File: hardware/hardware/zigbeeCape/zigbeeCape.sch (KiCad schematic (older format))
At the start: 2 parts

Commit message: LIbrary updates
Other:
- moved on the sheet: U?A, U?B
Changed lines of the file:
@@
 L Zigbee:CC1352R U?
 U 2 1 6062844D
-P 1450 1750
-F 0 "U?" H 1675 2765 50  0000 C CNN
-F 1 "CC1352R" H 1675 2674 50  0000 C CNN
-F 2 "" H 2050 2950 50  0001 C CNN
-F 3 "" H 2050 2950 50  0001 C CNN
-	2    1450 1750
+P 2600 4900
+F 0 "U?" H 2825 5915 50  0000 C CNN
+F 1 "CC1352R" H 2825 5824 50  0000 C CNN
+F 2 "" H 3200 6100 50  0001 C CNN
+F 3 "" H 3200 6100 50  0001 C CNN
+	2    2600 4900
 	1    0    0    -1
 $EndComp
@@
 L Zigbee:CC1352R U?
 U 1 1 60629828
-P 2950 1750
-F 0 "U?" H 3400 2765 50  0000 C CNN
-F 1 "CC1352R" H 3400 2674 50  0000 C CNN
-F 2 "" H 3550 2950 50  0001 C CNN
-F 3 "" H 3550 2950 50  0001 C CNN
-	1    2950 1750
+P 2100 1800
+F 0 "U?" H 2550 2815 50  0000 C CNN
+F 1 "CC1352R" H 2550 2724 50  0000 C CNN
+F 2 "" H 2700 3000 50  0001 C CNN
+F 3 "" H 2700 3000 50  0001 C CNN
+	1    2100 1800
 	1    0    0    -1
 $EndComp
+$Comp
+L power:+3.3V #PWR?
+U 1 1 606286D5
+P 1250 2100
+F 0 "#PWR?" H 1250 1950 50  0001 C CNN
+F 1 "+3.3V" H 1265 2273 50  0000 C CNN
+F 2 "" H 1250 2100 50  0001 C CNN
+F 3 "" H 1250 2100 50  0001 C CNN
+	1    1250 2100
+	1    0    0    -1
+$EndComp

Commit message: Forgot a file
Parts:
- added C? (x3): C, symbol Device:C
- added D?: Green, symbol Device:LED
- added D? (x3): Blue, symbol Device:LED
- added D?: RED, symbol Device:LED
- added R? (x5): 1k, symbol Device:R
- added SW? (x3): SW_MEC_5E, symbol Switch:SW_MEC_5E
- added U?: BeagleBone_P8, symbol BeagleBone:BeagleBone_P8
- added U?: BeagleBone_P9, symbol BeagleBone:BeagleBone_P9
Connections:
- net +3V3: now also D?.2 (A)
- new net: D?.1 (K), R?.1 (x5)
- new net Check_Error: C?.1, SW?.3 (K), SW?.4 (A)
- new net Error: D?.2 (A)
- new net GND: C?.2, C?.2, C?.2, R?.2, R?.2, R?.2, R?.2, R?.2, SW?.1, SW?.1, SW?.1, SW?.2, SW?.2, SW?.2
- new net Network_Connect: C?.1, SW?.3 (K), SW?.4 (A)
- new net Server_Status: D?.2 (A)
- new net ZigBee_Connect: C?.1, SW?.3 (K), SW?.4 (A)
- new net ZigBee_Receive: D?.2 (A)
- new net ZigBee_Transmit: D?.2 (A)
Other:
- note added: "LEDs and Buttons"
- moved on the sheet: U?B

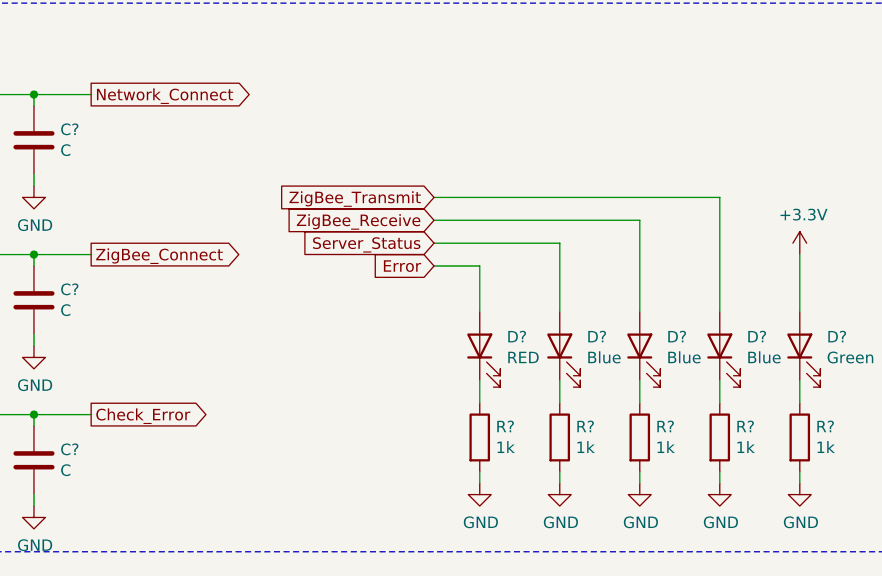
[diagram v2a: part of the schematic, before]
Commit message: Fixed LED names
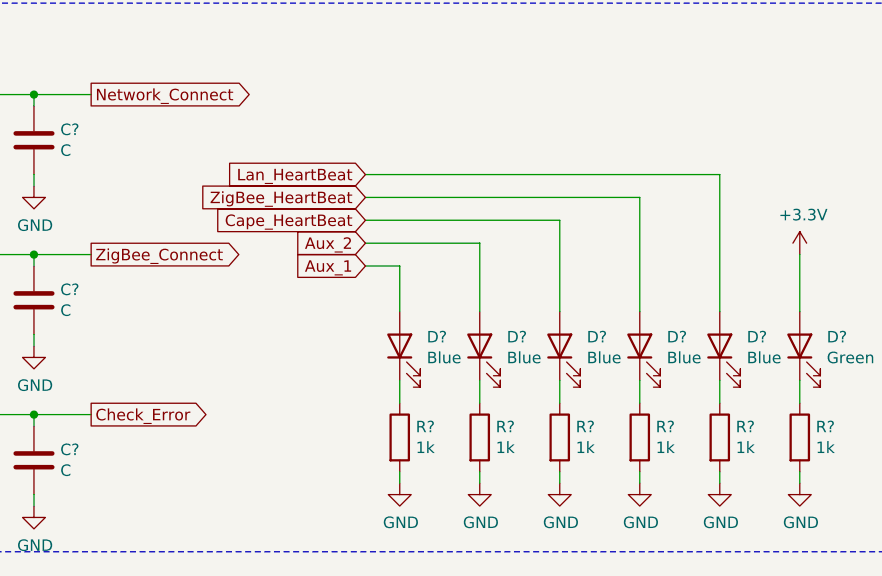
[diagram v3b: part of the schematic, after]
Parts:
- added D?: Blue, symbol Device:LED
- added R?: 1k, symbol Device:R
- D?: value RED -> Blue
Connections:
- net GND: now also R?.2
- net Error renamed Aux_2
- net Server_Status renamed Cape_HeartBeat
- net ZigBee_Receive renamed ZigBee_HeartBeat
- net ZigBee_Transmit renamed Lan_HeartBeat
- new net: D?.1 (K), R?.1
- new net Aux_1: D?.2 (A)
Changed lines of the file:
@@
 P 3600 6800
 F 0 "D?" V 3639 6682 50  0000 R CNN
-F 1 "RED" V 3548 6682 50  0000 R CNN
+F 1 "Blue" V 3548 6682 50  0000 R CNN
 F 2 "" H 3600 6800 50  0001 C CNN
 F 3 "~" H 3600 6800 50  0001 C CNN
@@
 	1650 7100 1900 7100
 Connection ~ 1650 7100
-Text GLabel 3400 6150 0    50   Input ~ 0
-ZigBee_Transmit
-Text GLabel 3400 6250 0    50   Input ~ 0
-ZigBee_Receive
-Text GLabel 3400 6350 0    50   Input ~ 0
-Server_Status
-Text GLabel 3400 6450 0    50   Input ~ 0
-Error
-Wire Wire Line
-	3400 6450 3600 6450
-Wire Wire Line
-	3600 6450 3600 6650
+Text GLabel 3100 6450 0    50   Input ~ 0
+Aux_1
 Wire Wire Line
 	3600 6950 3600 7050
@@
 Wire Wire Line
 	5000 7350 5000 7400
-Wire Wire Line
-	3950 6650 3950 6350
-Wire Wire Line
-	3950 6350 3400 6350
-Wire Wire Line
-	3400 6250 4300 6250
-Wire Wire Line
-	4300 6250 4300 6650
-Wire Wire Line
-	3400 6150 4650 6150
-Wire Wire Line
-	4650 6150 4650 6650
 $Comp
 L power:+3.3V #PWR?
@@
 Text Notes 600  5300 0    50   ~ 10
 LEDs and Buttons
+$Comp
+L Device:LED D?
+U 1 1 606BD4BD
+P 3250 6800
+F 0 "D?" V 3289 6682 50  0000 R CNN
+F 1 "Blue" V 3198 6682 50  0000 R CNN
+F 2 "" H 3250 6800 50  0001 C CNN
+F 3 "~" H 3250 6800 50  0001 C CNN
+	1    3250 6800
+	0    -1   -1   0
+$EndComp
+$Comp
+L Device:R R?
+U 1 1 606BD4C3
+P 3250 7200
+F 0 "R?" H 3320 7246 50  0000 L CNN
+F 1 "1k" H 3320 7155 50  0000 L CNN
+F 2 "" V 3180 7200 50  0001 C CNN
+F 3 "~" H 3250 7200 50  0001 C CNN
+	1    3250 7200
+	1    0    0    -1
+$EndComp
+$Comp
+L power:GND #PWR?
+U 1 1 606BD4C9
+P 3250 7400
+F 0 "#PWR?" H 3250 7150 50  0001 C CNN
+F 1 "GND" H 3255 7227 50  0000 C CNN
+F 2 "" H 3250 7400 50  0001 C CNN
+F 3 "" H 3250 7400 50  0001 C CNN
+	1    3250 7400
+	1    0    0    -1
+$EndComp
+Wire Wire Line
+	3250 6450 3250 6650
+Wire Wire Line
+	3250 6950 3250 7050
+Wire Wire Line
+	3250 7350 3250 7400
+Text GLabel 3100 6350 0    50   Input ~ 0
+Aux_2
+Wire Wire Line
+	3250 6450 3100 6450
+Text GLabel 3100 6050 0    50   Input ~ 0
+Lan_HeartBeat
+Text GLabel 3100 6150 0    50   Input ~ 0
+ZigBee_HeartBeat
+Text GLabel 3100 6250 0    50   Input ~ 0
+Cape_HeartBeat
+Wire Wire Line
+	3100 6350 3600 6350
+Wire Wire Line
+	3600 6350 3600 6650
+Wire Wire Line
+	3950 6650 3950 6250
+Wire Wire Line
+	3950 6250 3100 6250
+Wire Wire Line
+	3100 6150 4300 6150
+Wire Wire Line
+	4300 6150 4300 6650
+Wire Wire Line
+	3100 6050 4650 6050
+Wire Wire Line
+	4650 6050 4650 6650
 $EndSCHEMATC

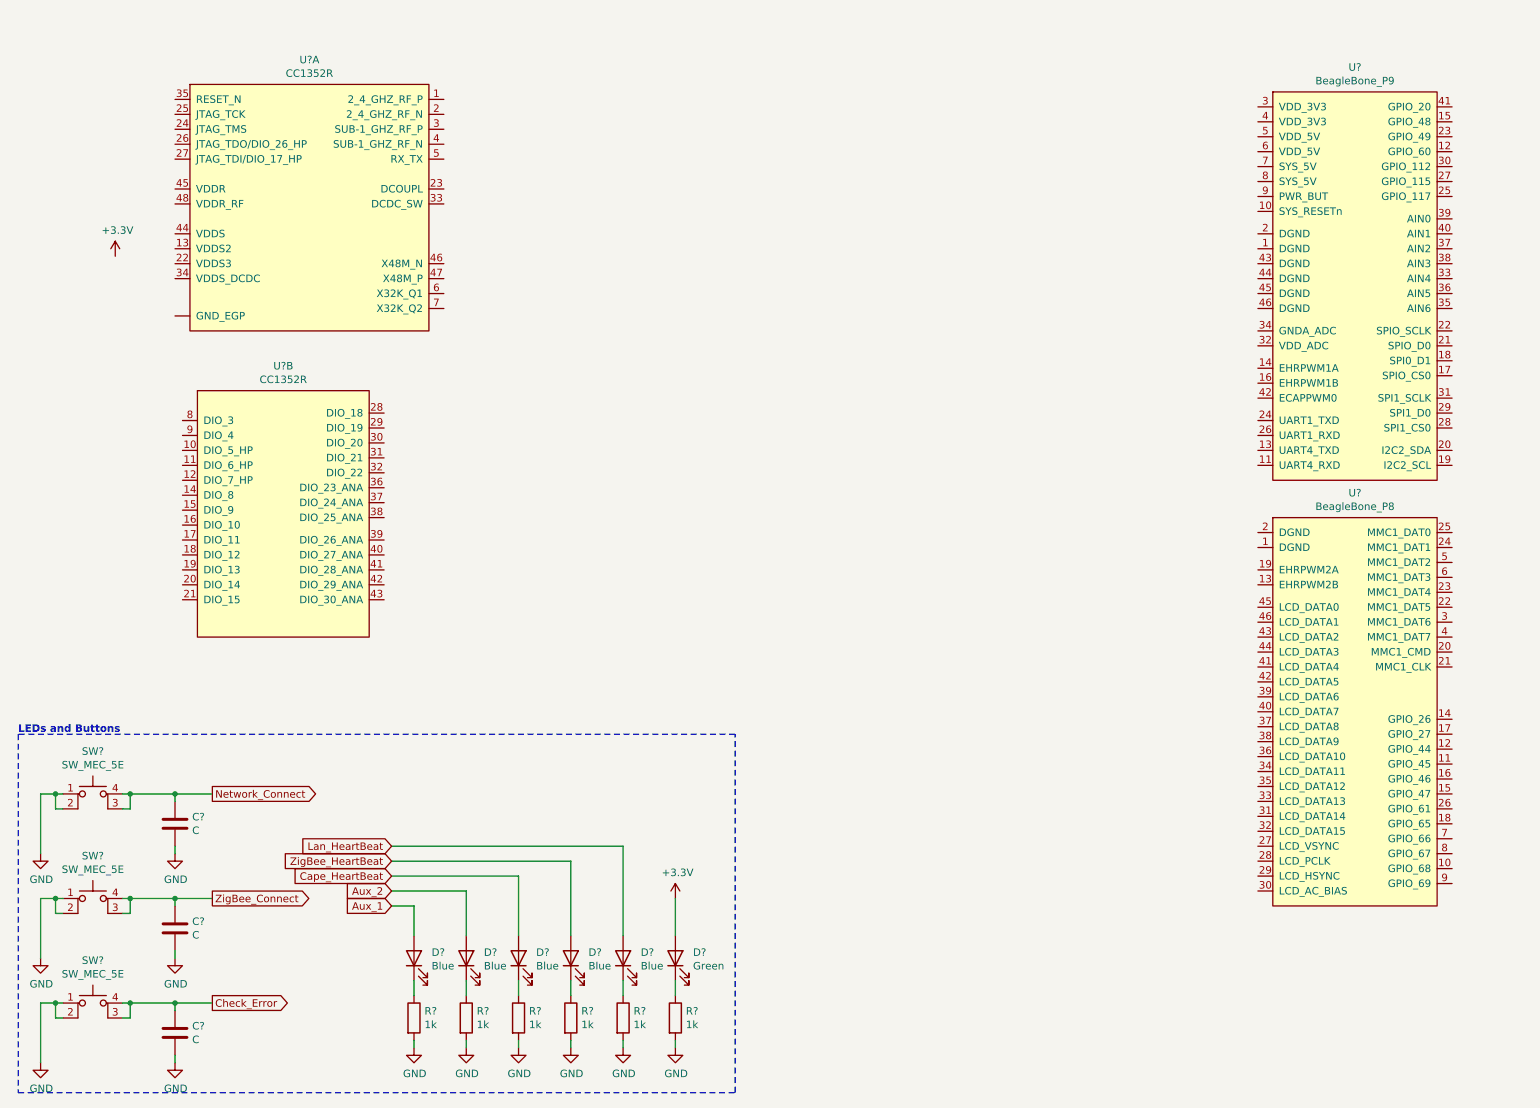
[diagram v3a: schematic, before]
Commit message: Added Most of Sub-1 Circuitry and most of Zigbee POwer Circuitry
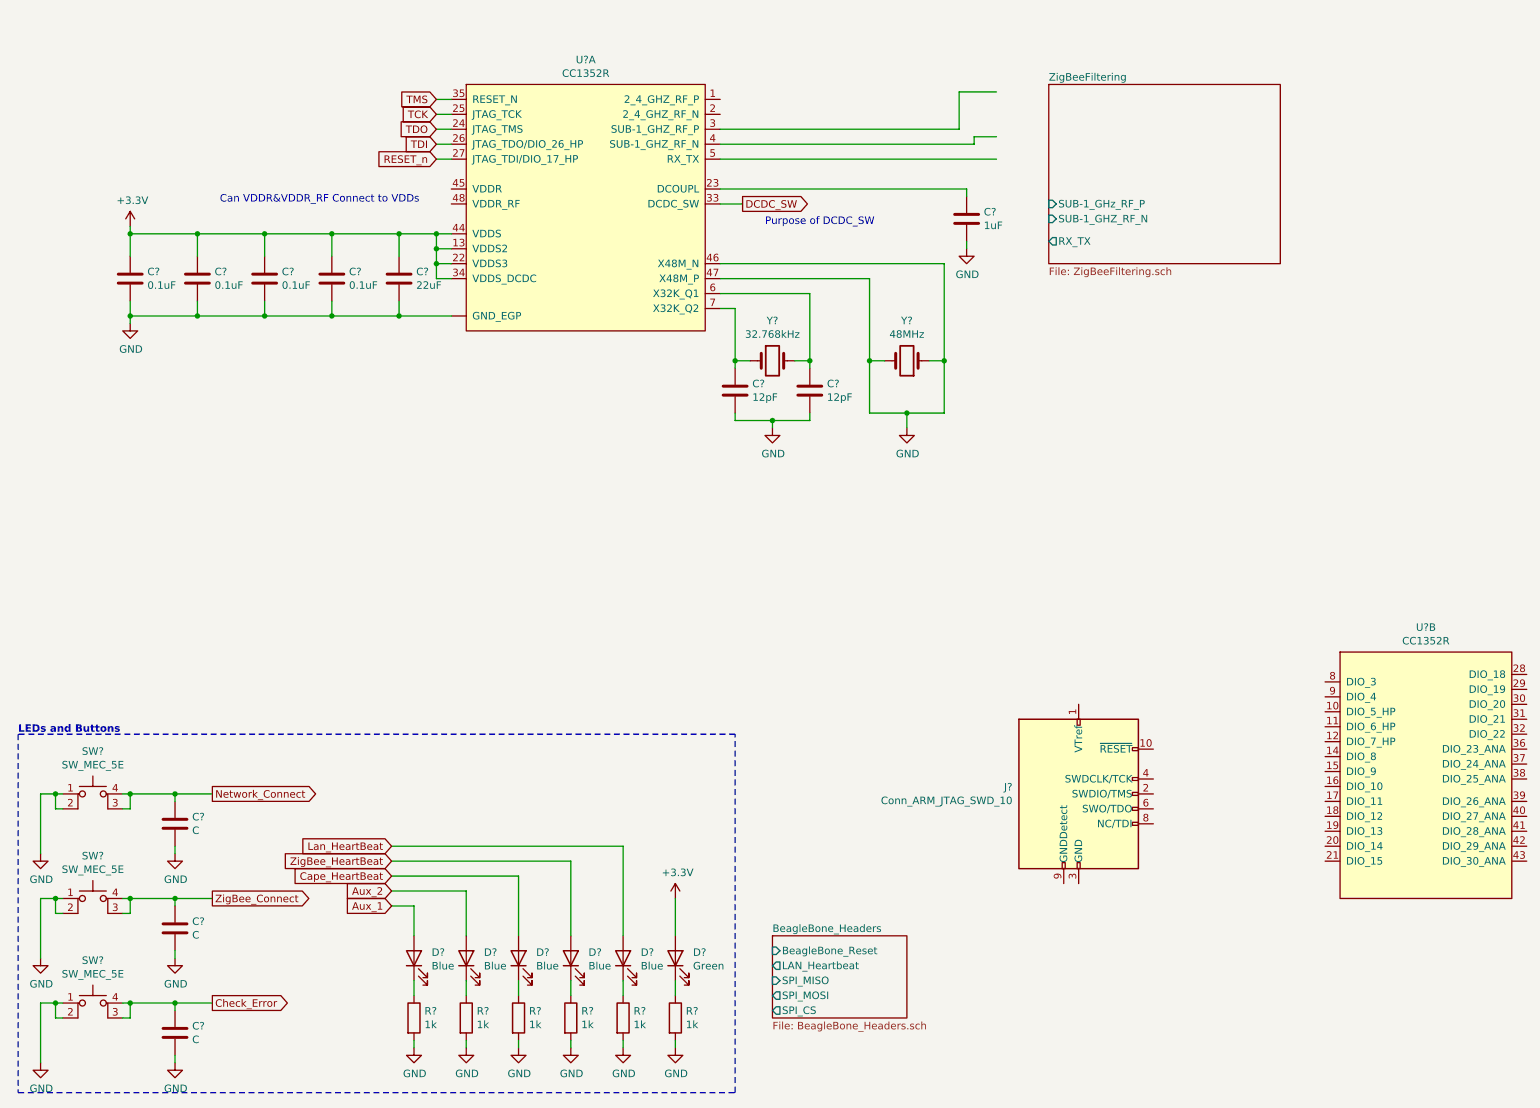
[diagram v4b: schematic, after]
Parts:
- removed U?: BeagleBone_P8, symbol BeagleBone:BeagleBone_P8
- removed U?: BeagleBone_P9, symbol BeagleBone:BeagleBone_P9
- added C?: 22uF, symbol Device:C
- added C? (x4): 0.1uF, symbol Device:C
- added C? (x2): 12pF, symbol Device:C
- added C?: 1uF, symbol Device:C
- added J?: Conn_ARM_JTAG_SWD_10, symbol Connector:Conn_ARM_JTAG_SWD_10
- added Y?: 32.768kHz, symbol Device:Crystal
- added Y?: 48MHz, symbol Device:Crystal
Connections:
- net +3V3: now also U?.13 (VDDS2), U?.22 (VDDS3), U?.34 (VDDS_DCDC), U?.44 (VDDS), C?.1, C?.1, C?.1, C?.1, C?.1
- net GND: now also U?.46 (X48M_N), U?.47 (X48M_P), U?.~ (GND_EGP), C?.2, C?.2, C?.2, C?.2, C?.2, C?.2, C?.2, C?.2, Y?.1, Y?.2
- net at U?.23 (DCOUPL): now also C?.1
- net TDO: now reaches U?.24 (JTAG_TMS)
- net TCK: now reaches U?.25 (JTAG_TCK)
- net TDI: now reaches U?.26 (JTAG_TDO/DIO_26_HP)
- net RESET_n: now reaches U?.27 (JTAG_TDI/DIO_17_HP)
- net DCDC_SW: now reaches U?.33 (DCDC_SW)
- net TMS: now reaches U?.35 (RESET_N)
- net at U?.6 (X32K_Q1): now also C?.1, Y?.2
- net at U?.7 (X32K_Q2): now also C?.1, Y?.1
- new net: J?.3 (GND), J?.5 (GND)
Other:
- note added: "Can VDDR&VDDR_RF Connect to VDDs\n"
- note added: "Purpose of DCDC_SW"
- moved on the sheet: U?A, U?B
